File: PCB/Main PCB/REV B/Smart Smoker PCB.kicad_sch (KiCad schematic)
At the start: 78 parts, among them J1 105017-0001, J3 393570002, J4 393570002, J5 393570002, J6 393570002, J7 393570002, J8 Hopper, J9 Lid, Q1 Q_PMOS_GSD, Q2 25V 1.5A Trans, Q3 25V 1.5A Trans, Q4 Q_PMOS_GSD, Q5 2N7002T-7-F, Q6 2N7002T-7-F, U1 ESP32-WROOM-32UE_16MB, U2 DG409LEDY-T1-GE3, U3 MAX31855KASA, U4 AMS1117-3.3, U5 CP2102N-Axx-xQFN28, U6 LTC4412xS6

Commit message: Added suggestions to Hardware Rev B
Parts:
- removed C13: 0.1uF 50V X7R 0603, Capacitor_SMD:C_0603_1608Metric, symbol Device:C
- removed JP1: Jumper_2_Open, Connector_PinHeader_2.54mm:PinHeader_1x02_P2.54mm_Vertical, symbol Jumper:Jumper_2_Open
- removed Q5, Q6: 2N7002T-7-F, Package_TO_SOT_SMD:SOT-23, symbol Transistor_FET:2N7002
- removed R12: 1kOhm 1% 0603, Resistor_SMD:R_0603_1608Metric, symbol Device:R_US
- removed R13, R7: 10K 1% 0603, Resistor_SMD:R_0603_1608Metric, symbol Device:R_US
- removed TP1: TestPoint_2Pole, TestPoint:TestPoint_2Pads_Pitch5.08mm_Drill1.3mm, symbol Connector:TestPoint_2Pole
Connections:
- no-connect marks 22 -> 23
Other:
- note added: "Add A/H/F RGB LED Add 2nd GPIO LED"
- note added: "Add GND connect for AC"
- note added: "CAN this go? Modify to interrupt 3v3 off of PP"
- note added: "Change Footprint"
- note added: "Change Footprint marking"
- note added: "Change footprint on TP Add TP for Pre-PP Add TP pin for GND Add TP Pin for int 1 hopper I2C / SPI TP"
- note added: "Change to smaller chip?"
- note added: "Modify footprints"
- note added: "Verify if this works"
- note added: "Verify if this works New circuit if not?"
- moved on the sheet: AE1, C1, C10, C11, C12, C14, C15, C16, C17, C18, C19, C2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

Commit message: Hardware Rev B in progress
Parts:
- removed C14: 0.1uF 50V X7R 0603, Capacitor_SMD:C_0603_1608Metric, symbol Device:C
- added D?: ASMB-KTF0-0A306, Customs Smoker:LED_ASMB-KTF0-0A306, symbol ASMB-KTF0-0A306:ASMB-KTF0-0A306
- added J?: MEM2051-00-195-00-A, Customs Smoker:GCT_MEM2051-00-195-00-A, symbol MEM2051-00-195-00-A:MEM2051-00-195-00-A
- added R?: 64.9Ohm 1% 0603, Resistor_SMD:R_0603_1608Metric, symbol Device:R_US
- added R? (x2): 20Ohm 1% 0603, Resistor_SMD:R_0603_1608Metric, symbol Device:R_US
- S1: value TL1015AF160QG -> UNK; footprint Customs Smoker:SW_TL1015AF160QG -> TestPoint:TestPoint_2Pads_Pitch5.08mm_Drill1.3mm; MANUFACTURER E-Switch -> (none); MAXIMUM_PACKAGE_HEIGHT 2.1 mm -> (none); Manufacturer E-Switch -> (none); Manufacturer Part Number TL1015AF160QG -> (none); PARTREV F -> (none); STANDARD Manufacturer Recommendations -> (none); Vendor Digikey -> (none); Vendor Part Number EG4344CT-ND -> (none)
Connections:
- net +3.3V: now also S1.1, S1.2, D?.1
- net GND: no longer S1.1
- net IO0: no longer S1.2
- net IO25: now also R?.2
- net IO26: now also R?.2
- net IO27: now also R?.2
- new net: D?.2, R?.1
- new net: D?.3, R?.1
- new net: D?.4, R?.1
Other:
- note added: "MAIN PWR"
- note added: "Verify if this works New circuit if not? https://www.digikey.ca/en/products/detail/recom-power/RAC05-3-3SK/7603369"
- note removed: "Add A/H/F RGB LED Add 2nd GPIO LED"
- note removed: "Boot"
- note removed: "CAN this go? Modify to interrupt 3v3 off of PP"
- note removed: "NC by Default"
- note removed: "Verify if this works New circuit if not?"
- moved on the sheet: C10, C12, Q1, Q4, R11, U6

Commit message: Hardware Rev B development
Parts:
- added C? (x2): 0.1uF 50V X7R 0603, Capacitor_SMD:C_0603_1608Metric, symbol Device:C
- added C?: 4.7uF 25V X5R 0805, Capacitor_SMD:C_0805_2012Metric, symbol Device:C
- added R?: 22.1kOhm 1% 0603, Resistor_SMD:R_0603_1608Metric, symbol Device:R_US
- added R?: 47.5kOhm 1% 0603, Resistor_SMD:R_0603_1608Metric, symbol Device:R_US
- added R?: 1kOhm 1% 0603, Resistor_SMD:R_0603_1608Metric, symbol Device:R_US
- added S?: TL1015AF160QG, Customs Smoker:SW_TL1015AF160QG, symbol TL1015AF160QG:TL1015AF160QG
- added TP? (x2): 3V3 TP, TestPoint:TestPoint_THTPad_D1.0mm_Drill0.5mm, symbol Connector:TestPoint
- added TP?: SDA TP, TestPoint:TestPoint_THTPad_D1.0mm_Drill0.5mm, symbol Connector:TestPoint
- added TP?: GPIO MISC., Connector_PinHeader_2.54mm:PinHeader_1x04_P2.54mm_Vertical, symbol Connector_Generic:Conn_01x04
- added TP?: GND TP PIN, Connector_PinHeader_2.54mm:PinHeader_1x01_P2.54mm_Vertical, symbol Connector:TestPoint
- added TP?: GND TP, TestPoint:TestPoint_THTPad_D1.0mm_Drill0.5mm, symbol Connector:TestPoint
- added TP?: SCL TP, TestPoint:TestPoint_THTPad_D1.0mm_Drill0.5mm, symbol Connector:TestPoint
- added U?: CP2102N-Axx-xQFN20, Package_DFN_QFN:QFN-24-1EP_4x4mm_P0.5mm_EP2.6x2.6mm, symbol Interface_USB:CP2102N-Axx-xQFN24
- TP2: value TestPoint_2Pole -> 3V3 TP; footprint TestPoint:TestPoint_2Pads_Pitch5.08mm_Drill1.3mm -> TestPoint:TestPoint_THTPad_D1.0mm_Drill0.5mm; symbol Connector:TestPoint_2Pole -> Connector:TestPoint
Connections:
- net +3.3V: now also C?.2, C?.2, R?.2, U?.6 (VDD), U?.7 (VREGIN)
- net +3.3VA: now also TP?.1
- net +3.3VP: now also TP?.1
- net +5V: now also R?.1
- net CTS: now also U?.18 (~{CTS})
- net DTR: now also U?.23 (~{DTR})
- net GND: now also C?.1, C?.1, C?.2, R?.1, S?.1, TP?.1, TP?.1, U?.2 (GND), U?.25 (GND); no longer TP2.2
- net I2C_SCL: now also TP?.1
- net I2C_SDA: now also TP?.1
- net IO0: now also C?.1, S?.2
- net RTS: now also U?.19 (~{RTS})
- net RXD: now also U?.20 (RXD)
- net TXD: now also U?.21 (TXD)
- net USB_DN: now also U?.4 (D-)
- net USB_DP: now also U?.3 (D+)
- new net: R?.2, R?.2, U?.8 (VBUS)
- new net: R?.1, U?.9 (~{RST})
- no-connect marks 23 -> 33
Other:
- note added: "Add boot button"
- note added: "BOOT"
- note removed: "Change footprint on TP Add TP for Pre-PP Add TP pin for GND Add TP Pin for int 1 hopper I2C / SPI TP"

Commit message: Hardware Rev B development - missing relays
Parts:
- removed C5: 0.1uF 50V X7R 0603, Capacitor_SMD:C_0603_1608Metric, symbol Device:C
- removed C6: 4.7uF 25V X5R 0805, Capacitor_SMD:C_0805_2012Metric, symbol Device:C
- removed Q4: Q_PMOS_GSD, Customs Smoker:VESM_TOS, symbol Device:Q_PMOS_GSD
- removed R10: 47.5kOhm 1% 0603, Resistor_SMD:R_0603_1608Metric, symbol Device:R_US
- removed R3: 1kOhm 1% 0603, Resistor_SMD:R_0603_1608Metric, symbol Device:R_US
- removed R5: 22.1kOhm 1% 0603, Resistor_SMD:R_0603_1608Metric, symbol Device:R_US
- removed S1: UNK, TestPoint:TestPoint_2Pads_Pitch5.08mm_Drill1.3mm, symbol TL1015AF160QG:TL1015AF160QG
- removed U5: CP2102N-Axx-xQFN28, Package_DFN_QFN:QFN-28-1EP_5x5mm_P0.5mm_EP3.35x3.35mm, symbol Interface_USB:CP2102N-Axx-xQFN28
- added C?: 0.1uF 50V X7R 0603, Capacitor_SMD:C_0603_1608Metric, symbol Device:C
- added C?: 10uF 16V X5R 0805, Capacitor_SMD:C_0805_2012Metric, symbol Device:C
- added MT?: PEC11R-4215F-S0024, Customs Smoker:XDCR_PEC11R-4215F-S0024, symbol PEC11R-4215F-S0024:PEC11R-4215F-S0024
- added PS?: RAC05-3.3SK, Converter_ACDC:Converter_ACDC_RECOM_RAC05-xxSK_THT, symbol Converter_ACDC:RAC05-3.3SK
- added Q?: Q_PMOS_GSD, Package_TO_SOT_SMD:SOT-23, symbol Device:Q_PMOS_GSD
- added S?: RR511D1121, Customs Smoker:E-SWITCH_RR511D1121, symbol RR511D1121:RR511D1121
- added TP?: Screen I2C, Connector_PinHeader_2.54mm:PinHeader_1x04_P2.54mm_Vertical, symbol Connector_Generic:Conn_01x04
- Q1: footprint Customs Smoker:VESM_TOS -> Package_TO_SOT_SMD:SOT-23; Manufacturer Part Number SSM3J56MFV,L3F -> SSM3J328R,LF; Vendor Part Number SSM3J56MFVL3FCT-ND -> SSM3J328RLFCT-ND
- U4: footprint Package_TO_SOT_SMD:TO-252-3_TabPin2 -> Package_TO_SOT_SMD:TO-252-2
- U?: Manufacturer (none) -> Silicon Labs; Manufacturer Part Number (none) -> CP2102N-A02-GQFN24; Vendor (none) -> Digikey; Vendor Part Number (none) -> 336-5887-ND
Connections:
- net +3.3V: now also U?.5 (VIO), Q?.2 (S), S?.1, S?.2, TP?.4 (Pin_4)
- net +3.3VA: now also Q?.3 (D)
- net GND: now also TP?.3 (Pin_3)
- net I2C_SCL: now also TP?.2 (Pin_2)
- net I2C_SDA: now also TP?.1 (Pin_1)
- net at U6.5 (GATE): now also Q?.1 (G)
- new net: C?.1, C?.2, PS?.4 (-Vout)
- new net: C?.1, C?.2, PS?.5 (+Vout)
- new net: MT?.S1 (SHIELD), MT?.S2 (SHIELD)
- no-connect marks 33 -> 17
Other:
- note added: "I2C 0X7C"
- note added: "SD card New AC/DC Switch on Rotary Encoder Relay x3 RGB Screen"
- note removed: "Add boot button"
- note removed: "Change Footprint"
- note removed: "Change to smaller chip?"
- note removed: "Modify footprints"
- moved on the sheet: C?, R?, U?

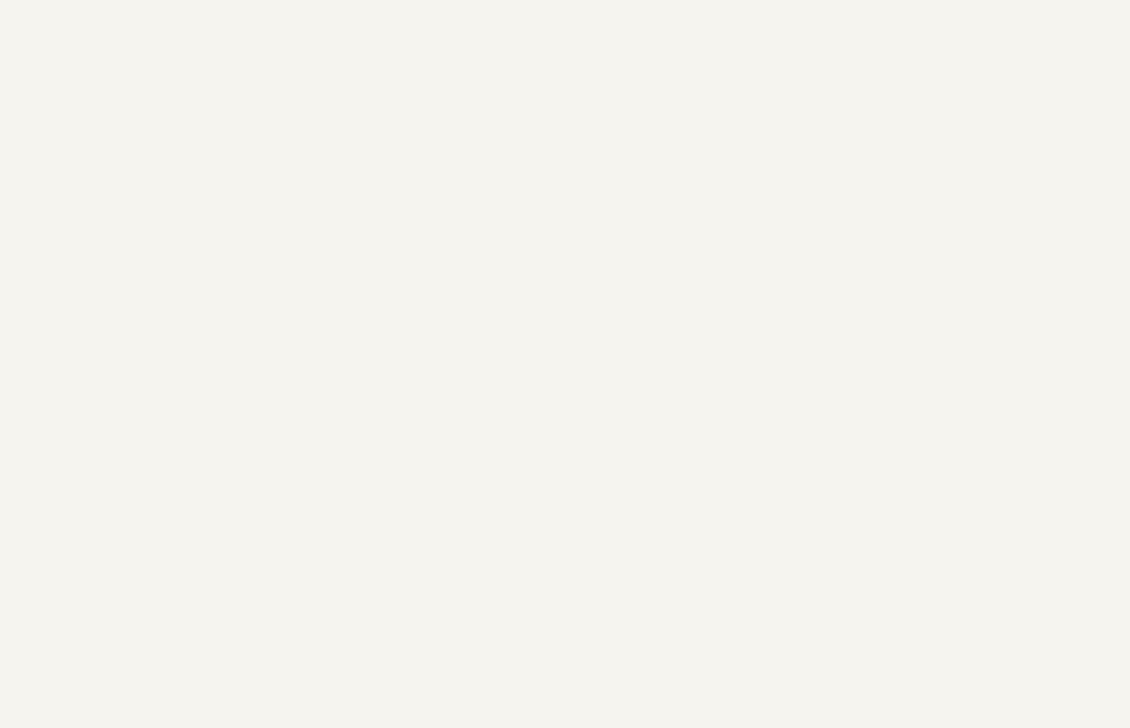
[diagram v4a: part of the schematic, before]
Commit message: Hardware Rev B development - 3/3 SSRs sourced
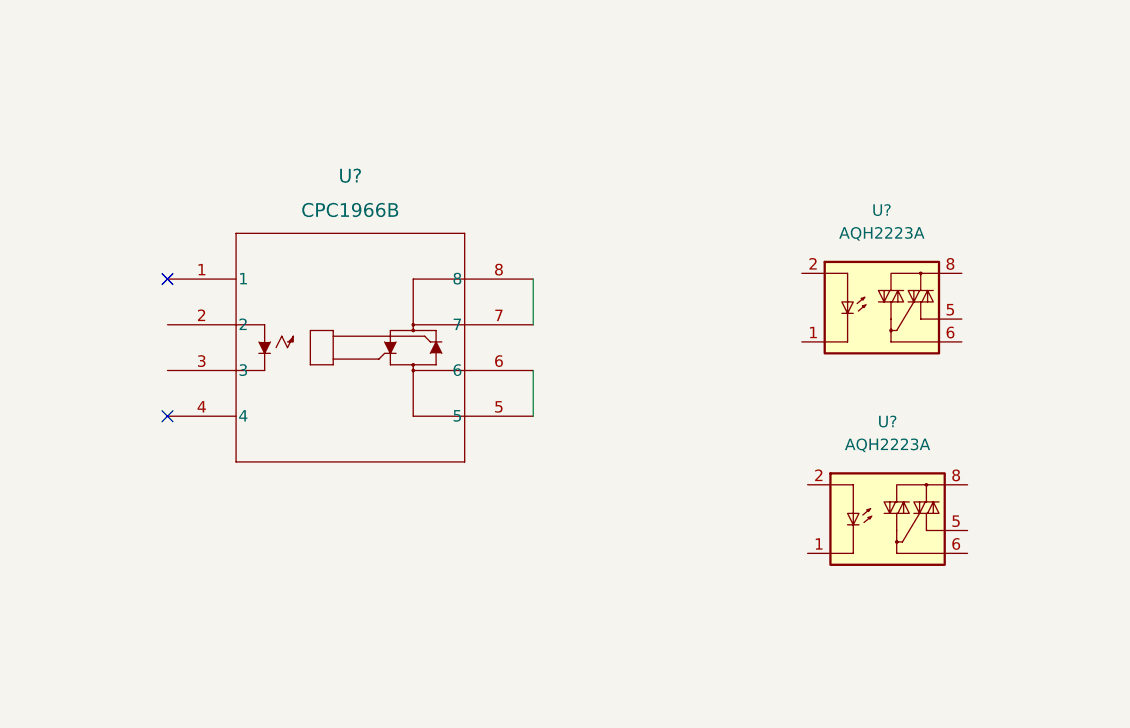
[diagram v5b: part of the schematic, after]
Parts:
- added U?: CPC1966B, Customs Smoker:CPC1966B_IXY, symbol CPC1966B:CPC1966B
- added U? (x2): AQH2223A, Package_SO:SSO-7-8_6.4x9.78mm_P2.54mm, symbol Relay_SolidState:AQH2223A
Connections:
- new net: U?.5, U?.6
- new net: U?.7, U?.8
- new net: U?.1, U?.3, U?.4 (x2)
- no-connect marks 17 -> 19
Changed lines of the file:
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@@
   (no_connect (at 661.67 53.975))
   (no_connect (at 229.87 152.4))
+  (no_connect (at 266.7 44.45))
   (no_connect (at 189.23 167.64))
   (no_connect (at 189.23 165.1))
@@
   (no_connect (at 661.67 46.355))
   (no_connect (at 734.695 83.185))
+  (no_connect (at 266.7 59.69))
   (no_connect (at 661.67 66.675))
   (no_connect (at 189.23 162.56))
@@
     (stroke (width 0) (type default) (color 0 0 0 0))
   )
+  (wire (pts (xy 307.34 44.45) (xy 307.34 49.53))
+    (stroke (width 0) (type default) (color 0 0 0 0))
+  )
   (wire (pts (xy 501.015 140.335) (xy 504.825 140.335))
     (stroke (width 0) (type default) (color 0 0 0 0))
@@
     (stroke (width 0) (type default) (color 0 0 0 0))
   )
+  (wire (pts (xy 307.34 54.61) (xy 307.34 59.69))
+    (stroke (width 0) (type default) (color 0 0 0 0))
+  )
   (wire (pts (xy 502.285 207.01) (xy 495.935 207.01))
     (stroke (width 0) (type default) (color 0 0 0 0))
@@
     (pin "2")
   )
+  (symbol (lib_id "CPC1966B:CPC1966B") (at 266.7 44.45 0) (unit 1)
+    (in_bom yes) (on_board yes) (fields_autoplaced)
+    (property "Reference" "U?" (id 0) (at 287.02 33.02 0)
+      (effects (font (size 1.524 1.524)))
+    )
+    (property "Value" "CPC1966B" (id 1) (at 287.02 36.83 0)
+      (effects (font (size 1.524 1.524)))
+    )
+    (property "Footprint" "Customs Smoker:CPC1966B_IXY" (id 2) (at 266.7 44.45 0)
+      (effects (font (size 1.27 1.27) italic) hide)
+    )
+    (property "Datasheet" "https://www.ixysic.com/home/pdfs.nsf/www/CPC1966B.pdf/$file/CPC1966B.pdf" (id 3) (at 266.7 44.45 0)
+      (effects (font (size 1.27 1.27) italic) hide)
+    )
+    (property "Manufacturer" "IXYS Integrated Circuits Division" (id 4) (at 266.7 44.45 0)
+      (effects (font (size 1.27 1.27)) hide)
+    )
+    (property "Manufacturer Part Number" "CPC1966B" (id 5) (at 266.7 44.45 0)
+      (effects (font (size 1.27 1.27)) hide)
+    )
+    (property "Vendor" "Digikey" (id 6) (at 266.7 44.45 0)
+      (effects (font (size 1.27 1.27)) hide)
+    )
+    (property "Vendor Part Number" "CPC1966B-ND" (id 7) (at 266.7 44.45 0)
+      (effects (font (size 1.27 1.27)) hide)
+    )
+    (pin "1")
+    (pin "2")
+    (pin "3")
+    (pin "4")
+    (pin "5")
+    (pin "6")
+    (pin "7")
+    (pin "8")
+  )
   (symbol (lib_id "power:+5V") (at 487.045 151.765 0) (unit 1)
     (in_bom yes) (on_board yes) (fields_autoplaced)
@@
     (pin "3")
   )
+  (symbol (lib_id "Relay_SolidState:AQH2223A") (at 347.345 46.355 0) (unit 1)
+    (in_bom yes) (on_board yes) (fields_autoplaced)
+    (property "Reference" "U?" (id 0) (at 346.075 36.83 0))
+    (property "Value" "AQH2223A" (id 1) (at 346.075 39.37 0))
+    (property "Footprint" "Package_SO:SSO-7-8_6.4x9.78mm_P2.54mm" (id 2) (at 339.725 51.435 0)
+      (effects (font (size 1.27 1.27) italic) (justify left) hide)
+    )
+    (property "Datasheet" "https://b2b-api.panasonic.eu/file_stream/pids/fileversion/2787" (id 3) (at 344.805 46.355 0)
+      (effects (font (size 1.27 1.27)) (justify left) hide)
+    )
+    (property "Manufacturer" "Panasonic Electric Works" (id 4) (at 347.345 46.355 0)
+      (effects (font (size 1.27 1.27)) hide)
+    )
+    (property "Manufacturer Part Number" "AQH2223AZ" (id 5) (at 347.345 46.355 0)
+      (effects (font (size 1.27 1.27)) hide)
+    )
+    (property "Vendor" "Digikey" (id 6) (at 347.345 46.355 0)
+      (effects (font (size 1.27 1.27)) hide)
+    )
+    (property "Vendor Part Number" "255-6000-1-ND" (id 7) (at 347.345 46.355 0)
+      (effects (font (size 1.27 1.27)) hide)
+    )
+    (pin "1")
+    (pin "2")
+    (pin "3")
+    (pin "4")
+    (pin "5")
+    (pin "6")
+    (pin "8")
+  )
   (symbol (lib_id "Device:R_US") (at 631.19 31.115 180) (unit 1)
     (in_bom yes) (on_board yes)
@@
     (pin "1")
   )
+  (symbol (lib_id "Relay_SolidState:AQH2223A") (at 347.98 69.85 0) (unit 1)
+    (in_bom yes) (on_board yes) (fields_autoplaced)
+    (property "Reference" "U?" (id 0) (at 346.71 60.325 0))
+    (property "Value" "AQH2223A" (id 1) (at 346.71 62.865 0))
+    (property "Footprint" "Package_SO:SSO-7-8_6.4x9.78mm_P2.54mm" (id 2) (at 340.36 74.93 0)
+      (effects (font (size 1.27 1.27) italic) (justify left) hide)
+    )
+    (property "Datasheet" "https://b2b-api.panasonic.eu/file_stream/pids/fileversion/2787" (id 3) (at 345.44 69.85 0)
+      (effects (font (size 1.27 1.27)) (justify left) hide)
+    )
+    (property "Manufacturer" "Panasonic Electric Works" (id 4) (at 347.98 69.85 0)
+      (effects (font (size 1.27 1.27)) hide)
+    )
+    (property "Manufacturer Part Number" "AQH2223AZ" (id 5) (at 347.98 69.85 0)
+      (effects (font (size 1.27 1.27)) hide)
+    )
+    (property "Vendor" "Digikey" (id 6) (at 347.98 69.85 0)
+      (effects (font (size 1.27 1.27)) hide)
+    )
+    (property "Vendor Part Number" "255-6000-1-ND" (id 7) (at 347.98 69.85 0)
+      (effects (font (size 1.27 1.27)) hide)
+    )
+    (pin "1")
+    (pin "2")
+    (pin "3")
+    (pin "4")
+    (pin "5")
+    (pin "6")
+    (pin "8")
+  )
   (symbol (lib_id "Device:C") (at 177.8 127 0) (mirror x) (unit 1)
     (in_bom yes) (on_board yes) (fields_autoplaced)
@@
       (reference "U?") (unit 1) (value "CP2102N-Axx-xQFN20") (footprint "Package_DFN_QFN:QFN-24-1EP_4x4mm_P0.5mm_EP2.6x2.6mm")
     )
+    (path "/99584623-e022-4536-b686-eb188d426f8e"
+      (reference "U?") (unit 1) (value "CPC1966B") (footprint "Customs Smoker:CPC1966B_IXY")
+    )
+    (path "/d0834f92-886f-48df-8410-4e3653f190bb"
+      (reference "U?") (unit 1) (value "AQH2223A") (footprint "Package_SO:SSO-7-8_6.4x9.78mm_P2.54mm")
+    )
+    (path "/f7292102-b150-47f5-8dae-8f71576a9014"
+      (reference "U?") (unit 1) (value "AQH2223A") (footprint "Package_SO:SSO-7-8_6.4x9.78mm_P2.54mm")
+    )
   )

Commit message: Hardware Rev B development
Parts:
- removed U?: AQH2223A, Package_SO:SSO-7-8_6.4x9.78mm_P2.54mm, symbol Relay_SolidState:AQH2223A
- added R? (x3): 140Ohm 1% 0603, Resistor_SMD:R_0603_1608Metric, symbol Device:R_US
- added R? (x3): 80.6Ohm 1% 0603, Resistor_SMD:R_0603_1608Metric, symbol Device:R_US
- added U?: AQH2223A, Package_SO:SSO-7-8_6.4x9.78mm_P2.54mm, symbol Relay_SolidState:AQH2223A
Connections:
- net GND: now also U?.1, U?.3, U?.3, U?.4, R?.2, R?.2, R?.2, U?.1, U?.3, U?.4
- net at U?.2: now also R?.1, R?.2 (x2)
- net Heater_-: now reaches U?.5, U?.6
- net Heater_+: now reaches U?.7, U?.8
- new net: R?.1, R?.2, U?.2
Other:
- note added: "RELAYS"
- note added: "ROTARY DIAL"
- note added: "SD CARD"
- moved on the sheet: U?

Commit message: Hardware Rev B development Relays and Rotary Encoder
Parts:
- removed MT?: PEC11R-4215F-S0024, Customs Smoker:XDCR_PEC11R-4215F-S0024, symbol PEC11R-4215F-S0024:PEC11R-4215F-S0024
- added D6, D7: D_TVS, Customs Smoker:DIOM7959X262N, symbol Device:D_TVS
- added J2: HEATER, TestPoint:TestPoint_2Pads_Pitch5.08mm_Drill1.3mm, symbol Connector_Generic:Conn_01x02
- added J4: AUGER, TestPoint:TestPoint_2Pads_Pitch5.08mm_Drill1.3mm, symbol Connector_Generic:Conn_01x02
- added J9: FAN, TestPoint:TestPoint_2Pads_Pitch5.08mm_Drill1.3mm, symbol Connector_Generic:Conn_01x02
- added SW1: SW_Coded_SH-7050, Rotary_Encoder:PAC18R1-43D19F, symbol Switch:SW_Coded_SH-7050
- gave numbers to parts that had none: 35
- renumbered C4 to C10, C2 to C11, C3 to C12, C15 to C13, C10 to C15, C12 to C16, C16 to C17, C17 to C18, C18 to C19, C19 to C20, C20 to C21, C7 to C5, C8 to C6, C9 to C7, C1 to C8, C11 to C9, D3 to D2, D4 to D3, D5 to D4, D2 to D8, J8 to J11, J9 to J12, J4 to J5, J5 to J6, J6 to J7, J7 to J8, PS1 to PS2, Q2 to Q1, Q3 to Q2, Q1 to Q3, R14 to R10, R17 to R11, R18 to R12, R19 to R14, R4 to R2, R11 to R21, R15 to R24, R16 to R25, R6 to R4, R8 to R6, R9 to R7, R1 to R8, R2 to R9, S2 to S1, TP2 to TP1, U4 to U1, U2 to U3, U3 to U4, U1 to U5, U6 to U8
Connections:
- net Heater_- is gone; now on net AC_L: U6.5, U6.6
- net AC_L: now also U7.6, U9.6, D6.2 (A2), D7.2 (A2)
- net AC_N: now also J2.2 (Pin_2), J4.2 (Pin_2), J9.2 (Pin_2)
- net Heater_+: now also J2.1 (Pin_1)
- net Fan_+: now reaches U9.8
- net Fan_+: now also D7.1 (A1), J9.1 (Pin_1)
- net Auger_+: now reaches U7.8
- net Auger_+: now also D6.1 (A1), J4.1 (Pin_1)
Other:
- moved on the sheet: R13, R15, R19, R20, R22, R23, TP1, TP2, TP3, TP4, TP5, TP6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

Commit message: Rev B Hardware - organization of schematic and initial layout for board sizing
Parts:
- removed C15: 1uF 25V X5R 0603, Capacitor_SMD:C_0603_1608Metric, symbol Device:C
- removed C16, C20, C3: 0.1uF 50V X7R 0603, Capacitor_SMD:C_0603_1608Metric, symbol Device:C
- removed C17: 22uF 450V 20%, Capacitor_THT:CP_Radial_D12.5mm_P5.00mm, symbol Device:C
- removed C18: 820uF 20% 16V, Capacitor_THT:CP_Radial_D10.0mm_P5.00mm, symbol Device:C
- removed C19: 150uF 20% 35V, Capacitor_THT:CP_Radial_D8.0mm_P3.50mm, symbol Device:C
- removed C21: 1000pF 440VAC Y5P, Capacitor_THT:C_Disc_D9.0mm_W5.0mm_P7.50mm, symbol Device:C
- removed C4, C5, C6, C7: 10uF 16V X5R 0805, Capacitor_SMD:C_0805_2012Metric, symbol Device:C
- removed D8: TVS DIODE 7VWM 12VC SMB, Diode_SMD:D_SMB, symbol Device:D_TVS
- removed F1: 300V 2A SlowBlow, Fuse:Fuse_Littelfuse_395Series, symbol Device:Fuse
- removed L1: 2.2mH 500mA 2.5Ohm TH, Inductor_THT:L_Radial_D10.5mm_P5.00mm_Abacron_AISR-01, symbol pspice:INDUCTOR
- removed L2: 2.2uH 7.2A 11.5mOhm, Inductor_SMD:L_Taiyo-Yuden_NR-80xx, symbol pspice:INDUCTOR
- removed PS1: RAC05-3.3SK, Converter_ACDC:Converter_ACDC_RECOM_RAC05-xxSK_THT, symbol Converter_ACDC:RAC05-3.3SK
- removed PS2: LS10-13B03R3, CONV_LS10-13B03R3, symbol LS10-13B03R3:LS10-13B03R3
- removed Q3, Q4: Q_PMOS_GSD, Package_TO_SOT_SMD:SOT-23, symbol Device:Q_PMOS_GSD
- removed R21: 470Ohm 5% 0603, Resistor_SMD:R_0603_1608Metric, symbol Device:R_US
- removed R24: 6.8Ohm 3W 5% 2512, Resistor_THT:R_Box_L8.4mm_W2.5mm_P5.08mm, symbol Device:R
- removed R25: B72214S0351K101, VARS_B72214S_15P5X5P6-7P5-2P2_TDK, symbol B72214S0351K101:B72214S0351K101
- removed S3: RR511D1121, Customs Smoker:E-SWITCH_RR511D1121, symbol RR511D1121:RR511D1121
- removed U1: AMS1117-3.3, Package_TO_SOT_SMD:TO-252-2, symbol Regulator_Linear:AMS1117-3.3
- removed U8: LTC4412xS6, Package_TO_SOT_SMD:TSOT-23-6, symbol Power_Management:LTC4412xS6
- added H1: AC_GND, MountingHole:MountingHole_3.2mm_M3_Pad_Via, symbol Mechanical:MountingHole_Pad
- renumbered C11 to C1, C1 to C11, C2 to C12, C9 to C14, C12 to C2, C8 to C3, C10 to C4, C13 to C5, C14 to C6, D1 to D6, D6 to D7, D7 to D8, H1 to H2, H2 to H3, H3 to H4, H4 to H5, J2 to J1, J9 to J10, J12 to J11, J10 to J12, J1 to J2, J5 to J4, J4 to J5, J11 to J9, R8 to R1, R4 to R10, R14 to R11, R13 to R12, R3 to R13, R16 to R14, R17 to R15, R15 to R16, R18 to R17, R6 to R18, R5 to R19, R9 to R2, R7 to R20, R19 to R21, R20 to R22, R22 to R23, R23 to R24, R10 to R3, R11 to R5, R2 to R6, R1 to R8, R12 to R9, U5 to U1, U3 to U2, U4 to U3, U6 to U4, U2 to U5, U7 to U6, U9 to U7
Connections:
- net GND: now also H1.1
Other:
- added sheet Power (power.kicad_sch)
- note added: "Change to vertical"
- note added: "MOUNTING"
- note removed: "AC/DC"
- note removed: "Add GND connect for AC"
- note removed: "Change Footprint marking"
- note removed: "MAIN PWR"
- note removed: "Powerpath"
- note removed: "SD card New AC/DC Switch on Rotary Encoder Relay x3 RGB Screen"
- note removed: "Verify if this works"
- note removed: "Verify if this works New circuit if not? https://www.digikey.ca/en/products/detail/recom-power/RAC05-3-3SK/7603369"
- moved on the sheet: AE1, C1, C11, C12, C14, C2, C3, C4, C5, C6, D2, D3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
